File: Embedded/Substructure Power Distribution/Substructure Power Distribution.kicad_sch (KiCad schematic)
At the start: 5 parts, among them J1 S JST, J2 D0 FFC, J3 D1 FFC, J4 S Pins A, J5 S Pins B

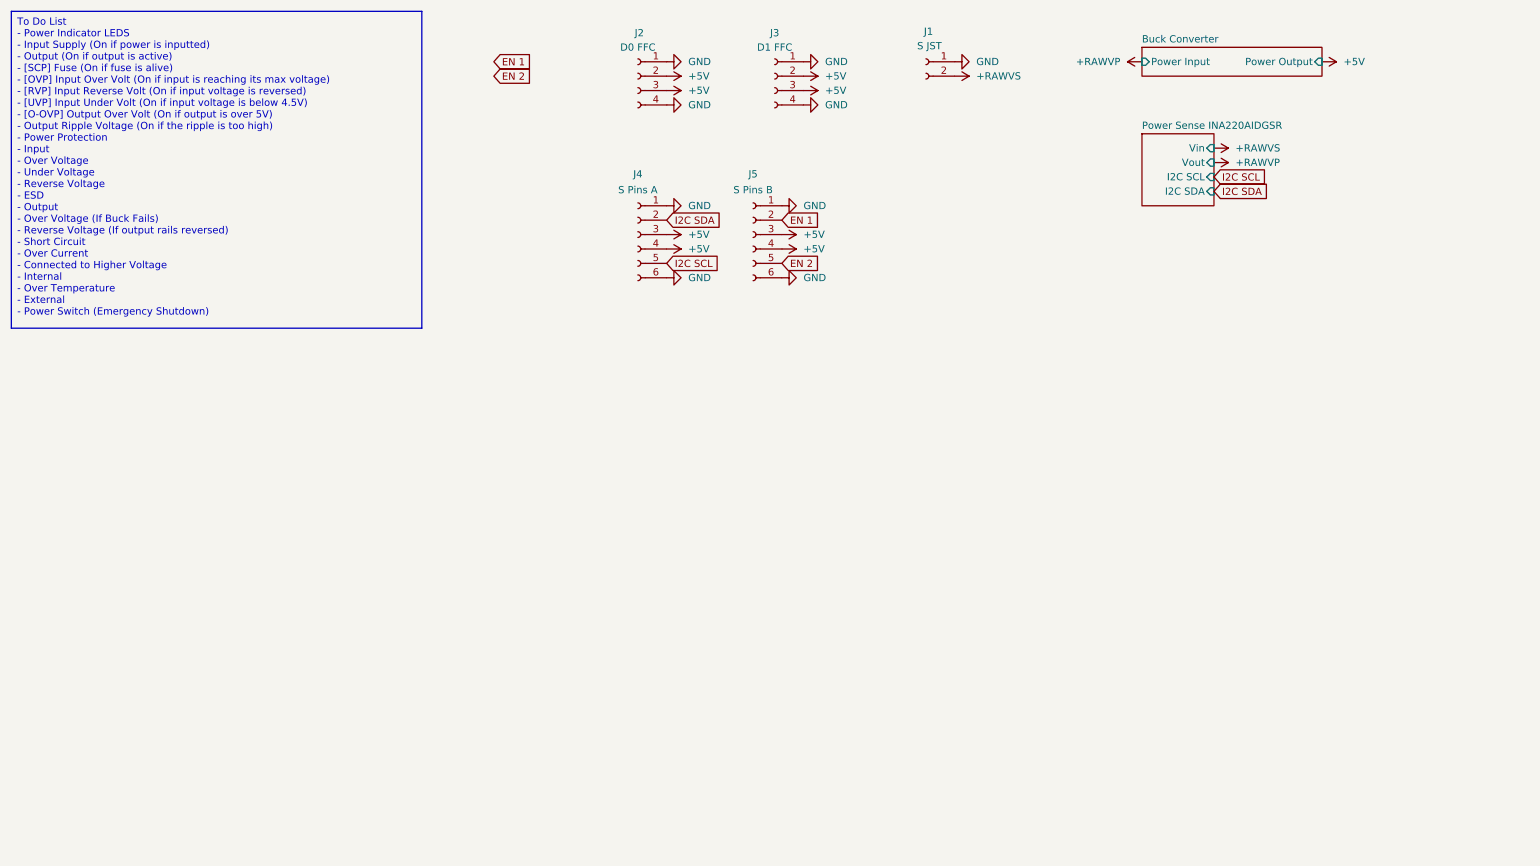
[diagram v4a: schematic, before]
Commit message: Added P Channel mosfets & crow bar circuits
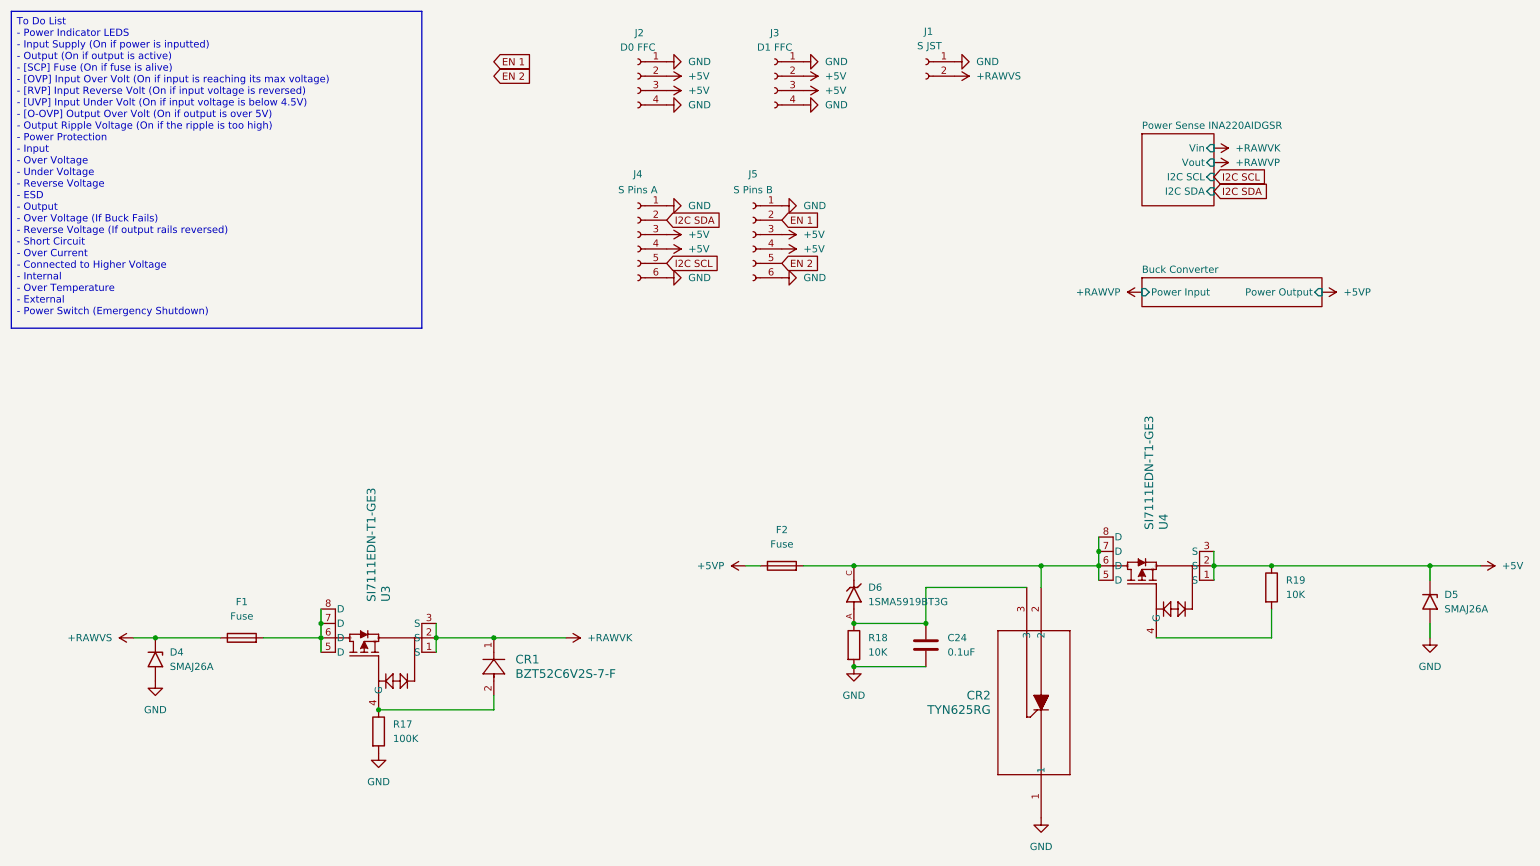
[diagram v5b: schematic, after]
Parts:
- added C24: 0.1uF, symbol Device:C
- added CR1: BZT52C6V2S-7-F, Zener Diode:SOD323_DIO, symbol Zener Diode:BZT52C6V2S-7-F
- added CR2: TYN625RG, Thyristor TYN:TO-220AB_STM, symbol Thyristor TYN:TYN625RG
- added D4, D5: SMAJ26A, Diode_SMD:D_SMA, symbol Diode:SMAJ26A
- added D6: 1SMA5919BT3G, Zener Diode:DIOM5226X220N, symbol Zener Diode 1SMA:1SMA5919BT3G
- added F1, F2: Fuse, Fuse:Fuse_1206_3216Metric_Pad1.42x1.75mm_HandSolder, symbol Device:Fuse
- added R17: 100K, symbol Device:R
- added R18, R19: 10K, symbol Device:R
- added U3, U4: SI7111EDN-T1-GE3, P Channel Mosfet:MOSFET_0DN-T1-GE3_VIS, symbol P Channel Mosfet:SI7111EDN-T1-GE3
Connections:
- net +5V: now also D5.1 (A1), R19.1, U4.1 (S), U4.2 (S), U4.3 (S)
- net +RAWVS: now also D4.1 (A1), F1.1
- net GND: now also C24.2, CR2.1, D4.2 (A2), D5.2 (A2), R17.2, R18.2
- new net: CR2.2, D6.C, F2.2, U4.5 (D), U4.6 (D), U4.7 (D), U4.8 (D)
- new net: CR1.2, R17.1, U3.4 (G)
- new net: R19.2, U4.4 (G)
- new net: F1.2, U3.5 (D), U3.6 (D), U3.7 (D), U3.8 (D)
- new net: C24.1, CR2.3, D6.A, R18.1
- new net +5VP: F2.1
- new net +RAWVK: CR1.1, U3.1 (S), U3.2 (S), U3.3 (S)

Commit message: Added Enable Pins
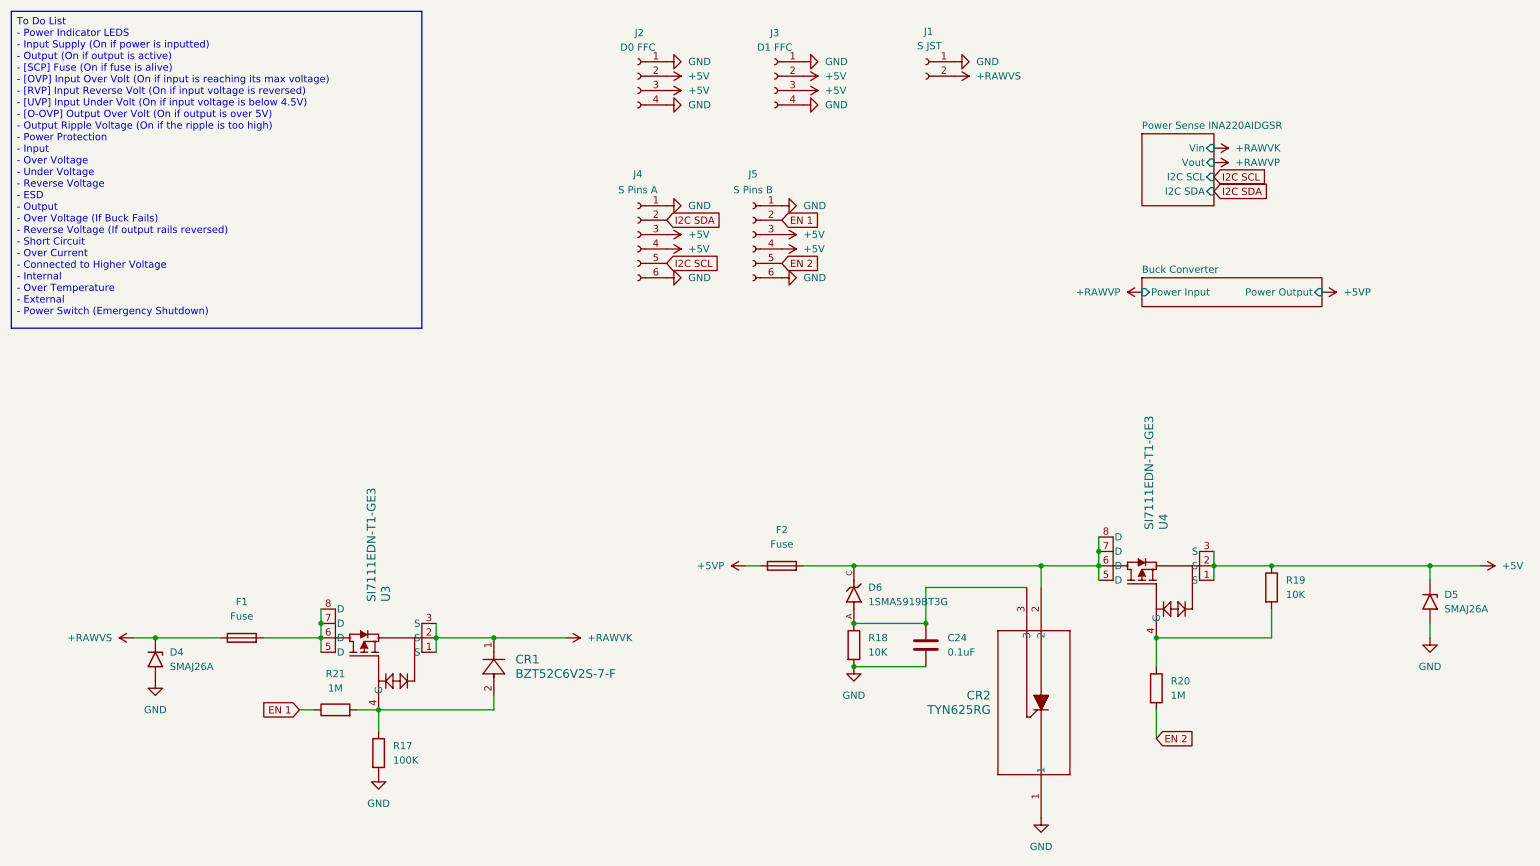
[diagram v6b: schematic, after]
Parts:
- added R20, R21: 1M, symbol Device:R
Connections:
- net EN 1: now also R21.1
- net EN 2: now also R20.2
- net at CR1.2, R17.1, U3.4 (G): now also R21.2
- net at R19.2, U4.4 (G): now also R20.1
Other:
- moved on the sheet: R17
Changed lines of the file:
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@@
+	)
+	(junction
+		(at 218.44 127)
+		(diameter 0)
+		(color 0 0 0 0)
 	)
 	(junction
@@
 	(wire
 		(pts
+			(xy 67.31 139.7) (xy 69.85 139.7)
+		)
+		(stroke
+			(width 0)
+			(type default)
+		)
+	)
+	(wire
+		(pts
 			(xy 266.7 114.3) (xy 275.59 114.3)
 		)
@@
 	(wire
 		(pts
+			(xy 77.47 139.7) (xy 81.28 139.7)
+		)
+		(stroke
+			(width 0)
+			(type default)
+		)
+	)
+	(wire
+		(pts
 			(xy 228.6 116.84) (xy 228.6 114.3)
 		)
@@
 	(wire
 		(pts
+			(xy 218.44 144.78) (xy 218.44 139.7)
+		)
+		(stroke
+			(width 0)
+			(type default)
+		)
+	)
+	(wire
+		(pts
 			(xy 71.12 129.54) (xy 71.12 127)
 		)
@@
 	(wire
 		(pts
+			(xy 218.44 132.08) (xy 218.44 127)
+		)
+		(stroke
+			(width 0)
+			(type default)
+		)
+	)
+	(wire
+		(pts
 			(xy 60.96 127) (xy 71.12 127)
 		)
@@
 		(pts
 			(xy 165.1 132.08) (xy 177.8 132.08)
+		)
+		(stroke
+			(width 0)
+			(type default)
+		)
+	)
+	(wire
+		(pts
+			(xy 81.28 143.51) (xy 81.28 139.7)
 		)
 		(stroke
@@
 	(global_label "EN 2"
 		(shape input)
-		(at 101.6 27.94 0)
+		(at 218.44 144.78 0)
 		(fields_autoplaced yes)
 		(effects
@@
 		)
 		(property "Intersheetrefs" "${INTERSHEET_REFS}"
-			(at 109.2418 27.94 0)
+			(at 226.0818 144.78 0)
 			(effects
 				(font
@@
 	(global_label "EN 1"
 		(shape input)
-		(at 101.6 25.4 0)
+		(at 67.31 139.7 180)
 		(fields_autoplaced yes)
 		(effects
@@
 				(size 1.27 1.27)
 			)
-			(justify left)
+			(justify right)
 		)
 		(property "Intersheetrefs" "${INTERSHEET_REFS}"
-			(at 109.2418 25.4 0)
-			(effects
-				(font
-					(size 1.27 1.27)
-				)
-				(justify left)
+			(at 59.6682 139.7 0)
+			(effects
+				(font
+					(size 1.27 1.27)
+				)
+				(justify right)
 				(hide yes)
 			)
@@
 	(symbol
 		(lib_id "Device:R")
-		(at 81.28 143.51 0)
+		(at 81.28 147.32 0)
 		(unit 1)
 		(exclude_from_sim no)
@@
 		(fields_autoplaced yes)
 		(property "Reference" "R17"
-			(at 83.82 142.2399 0)
+			(at 83.82 146.0499 0)
 			(effects
 				(font
@@
 		)
 		(property "Value" "100K"
-			(at 83.82 144.7799 0)
+			(at 83.82 148.5899 0)
 			(effects
 				(font
@@
 		)
 		(property "Footprint" ""
-			(at 79.502 143.51 90)
+			(at 79.502 147.32 90)
 			(effects
 				(font
@@
 		)
 		(property "Datasheet" "~"
-			(at 81.28 143.51 0)
+			(at 81.28 147.32 0)
 			(effects
 				(font
@@
 		)
 		(property "Description" "Resistor"
-			(at 81.28 143.51 0)
+			(at 81.28 147.32 0)
 			(effects
 				(font
@@
 				(path "/6e7c3700-4b7d-4b10-b755-ccb609125a98"
 					(reference "R19")
+					(unit 1)
+				)
+			)
+		)
+	)
+	(symbol
+		(lib_id "Device:R")
+		(at 218.44 135.89 0)
+		(unit 1)
+		(exclude_from_sim no)
+		(in_bom yes)
+		(on_board yes)
+		(dnp no)
+		(fields_autoplaced yes)
+		(property "Reference" "R20"
+			(at 220.98 134.6199 0)
+			(effects
+				(font
+					(size 1.27 1.27)
+				)
+				(justify left)
+			)
+		)
+		(property "Value" "1M"
+			(at 220.98 137.1599 0)
+			(effects
+				(font
+					(size 1.27 1.27)
+				)
+				(justify left)
+			)
+		)
+		(property "Footprint" ""
+			(at 216.662 135.89 90)
+			(effects
+				(font
+					(size 1.27 1.27)
+				)
+				(hide yes)
+			)
+		)
+		(property "Datasheet" "~"
+			(at 218.44 135.89 0)
+			(effects
+				(font
+					(size 1.27 1.27)
+				)
+				(hide yes)
+			)
+		)
+		(property "Description" "Resistor"
+			(at 218.44 135.89 0)
+			(effects
+				(font
+					(size 1.27 1.27)
+				)
+				(hide yes)
+			)
+		)
+		(pin "2"
+		)
+		(pin "1"
+		)
+		(instances
+			(project "Substructure Power Distribution"
+				(path "/6e7c3700-4b7d-4b10-b755-ccb609125a98"
+					(reference "R20")
 					(unit 1)
 				)
@@
 	(symbol
 		(lib_id "power:GND")
-		(at 81.28 147.32 0)
+		(at 81.28 151.13 0)
 		(unit 1)
 		(exclude_from_sim no)
@@
 		(fields_autoplaced yes)
 		(property "Reference" "#PWR046"
-			(at 81.28 153.67 0)
+			(at 81.28 157.48 0)
 			(effects
 				(font
@@
 		)
 		(property "Value" "GND"
-			(at 81.28 152.4 0)
+			(at 81.28 156.21 0)
 			(effects
 				(font
@@
 		)
 		(property "Footprint" ""
-			(at 81.28 147.32 0)
+			(at 81.28 151.13 0)
 			(effects
 				(font
@@
 		)
 		(property "Datasheet" ""
-			(at 81.28 147.32 0)
+			(at 81.28 151.13 0)
 			(effects
 				(font
@@
 		)
 		(property "Description" "Power symbol creates a global label with name \"GND\" , ground"
-			(at 81.28 147.32 0)
+			(at 81.28 151.13 0)
 			(effects
 				(font
@@
 					(unit 1)
 				)
+			)
+		)
+	)
+	(symbol
+		(lib_id "Device:R")
+		(at 73.66 139.7 90)
+		(unit 1)
+		(exclude_from_sim no)
+		(in_bom yes)
+		(on_board yes)
+		(dnp no)
+		(fields_autoplaced yes)
+		(property "Reference" "R21"
+			(at 73.66 133.35 90)
+			(effects
+				(font
+					(size 1.27 1.27)
+				)
+			)
+		)
+		(property "Value" "1M"
+			(at 73.66 135.89 90)
+			(effects
+				(font
+					(size 1.27 1.27)
+				)
+			)
+		)
+		(property "Footprint" ""
+			(at 73.66 141.478 90)
+			(effects
+				(font
+					(size 1.27 1.27)
+				)
+				(hide yes)
+			)
+		)
+		(property "Datasheet" "~"
+			(at 73.66 139.7 0)
+			(effects
+				(font
+					(size 1.27 1.27)
+				)
+				(hide yes)
+			)
+		)
+		(property "Description" "Resistor"
+			(at 73.66 139.7 0)
+			(effects
+				(font
+					(size 1.27 1.27)
+				)
+				(hide yes)
+			)
+		)
+		(pin "2"
+		)
+		(pin "1"
+		)
+		(instances
+			(project "Substructure Power Distribution"
+				(path "/6e7c3700-4b7d-4b10-b755-ccb609125a98"
+					(reference "R21")
+					(unit 1)
+				)

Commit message: Added Component footprints
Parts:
- C24: footprint (none) -> Capacitor_SMD:C_0402_1005Metric_Pad0.74x0.62mm_HandSolder
- R17, R18, R19, R20, R21: footprint (none) -> Resistor_SMD:R_0402_1005Metric_Pad0.72x0.64mm_HandSolder
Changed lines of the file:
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@@
 			)
 		)
-		(property "Footprint" ""
+		(property "Footprint" "Resistor_SMD:R_0402_1005Metric_Pad0.72x0.64mm_HandSolder"
 			(at 79.502 147.32 90)
 			(effects
@@
 			)
 		)
-		(property "Footprint" ""
+		(property "Footprint" "Resistor_SMD:R_0402_1005Metric_Pad0.72x0.64mm_HandSolder"
 			(at 236.982 118.11 90)
 			(effects
@@
 			)
 		)
-		(property "Footprint" ""
+		(property "Footprint" "Resistor_SMD:R_0402_1005Metric_Pad0.72x0.64mm_HandSolder"
 			(at 216.662 135.89 90)
 			(effects
@@
 			)
 		)
-		(property "Footprint" ""
+		(property "Footprint" "Resistor_SMD:R_0402_1005Metric_Pad0.72x0.64mm_HandSolder"
 			(at 163.322 128.27 90)
 			(effects
@@
 			)
 		)
-		(property "Footprint" ""
+		(property "Footprint" "Resistor_SMD:R_0402_1005Metric_Pad0.72x0.64mm_HandSolder"
 			(at 73.66 141.478 90)
 			(effects
@@
 			)
 		)
-		(property "Footprint" ""
+		(property "Footprint" "Capacitor_SMD:C_0402_1005Metric_Pad0.74x0.62mm_HandSolder"
 			(at 178.7652 132.08 0)
 			(effects
